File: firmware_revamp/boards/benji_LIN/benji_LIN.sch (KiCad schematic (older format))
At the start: 37 parts, among them J1 CONN_02X03, J2 Conn_01x11, J3 Conn_01x11, J4 CONN_01X03, J5 CONN_01x02, J6 CONN_01X03, SW1 SW_Push_SPST_NO, U1 MCP2561-E_SN, U2 ATMEGA16M1, U3 TLIN1021DRQ1, Y1 Crystal_SMD

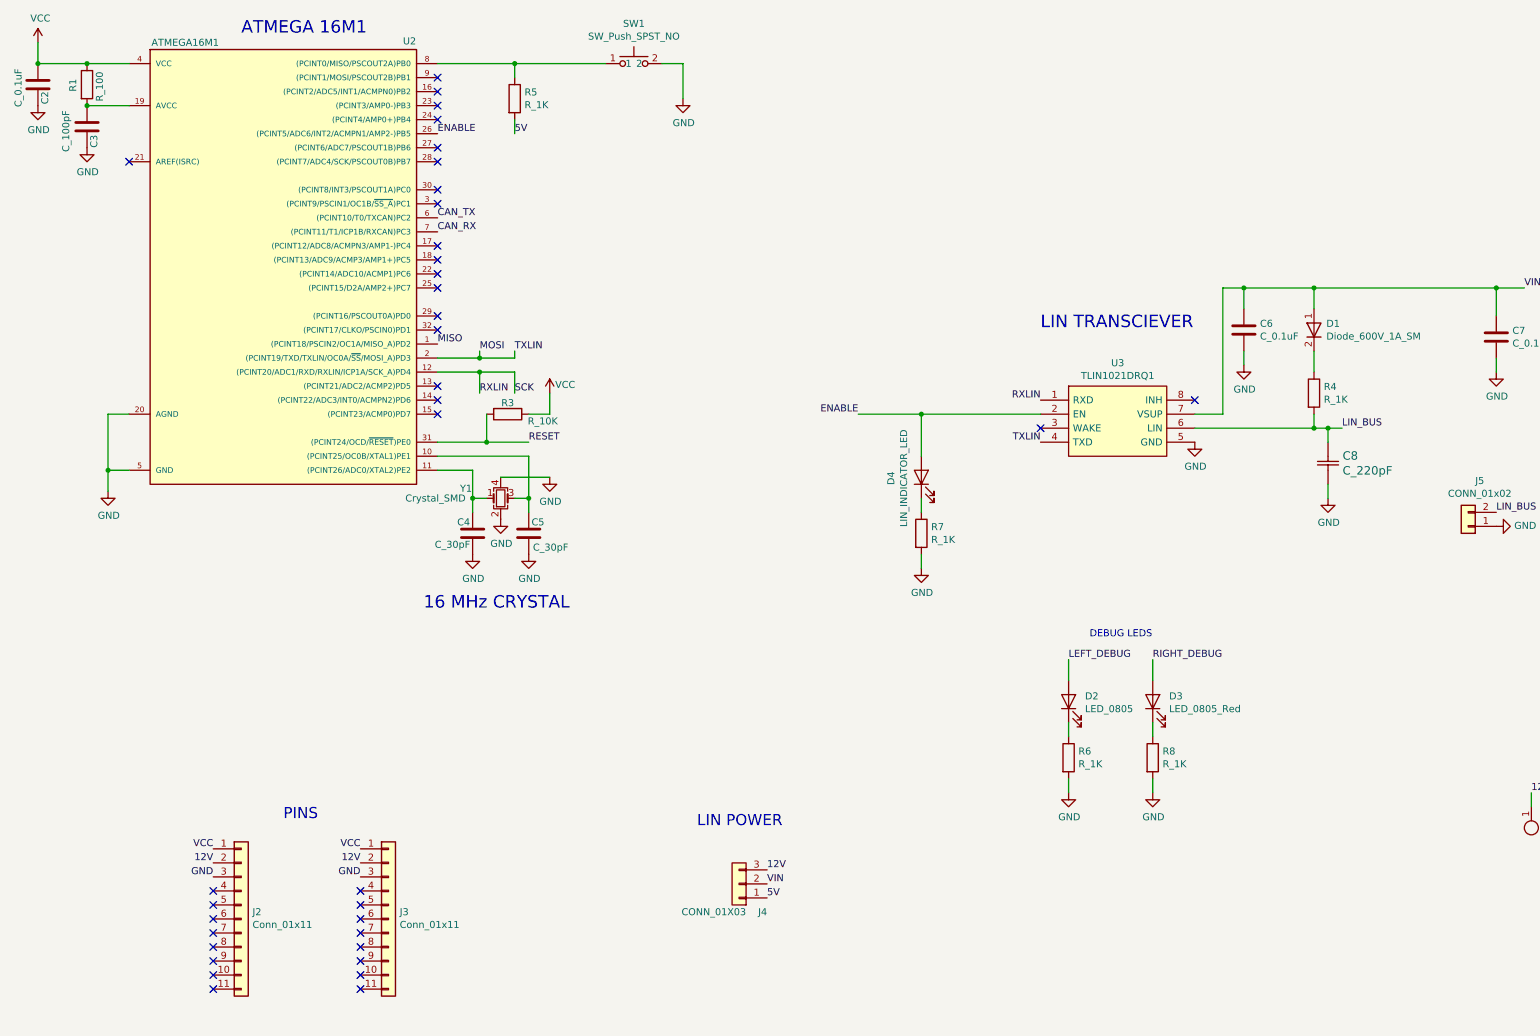
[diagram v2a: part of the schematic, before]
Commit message: Amended and finished up layout
assigned pins to headers, changed diode to led on LIN transciever
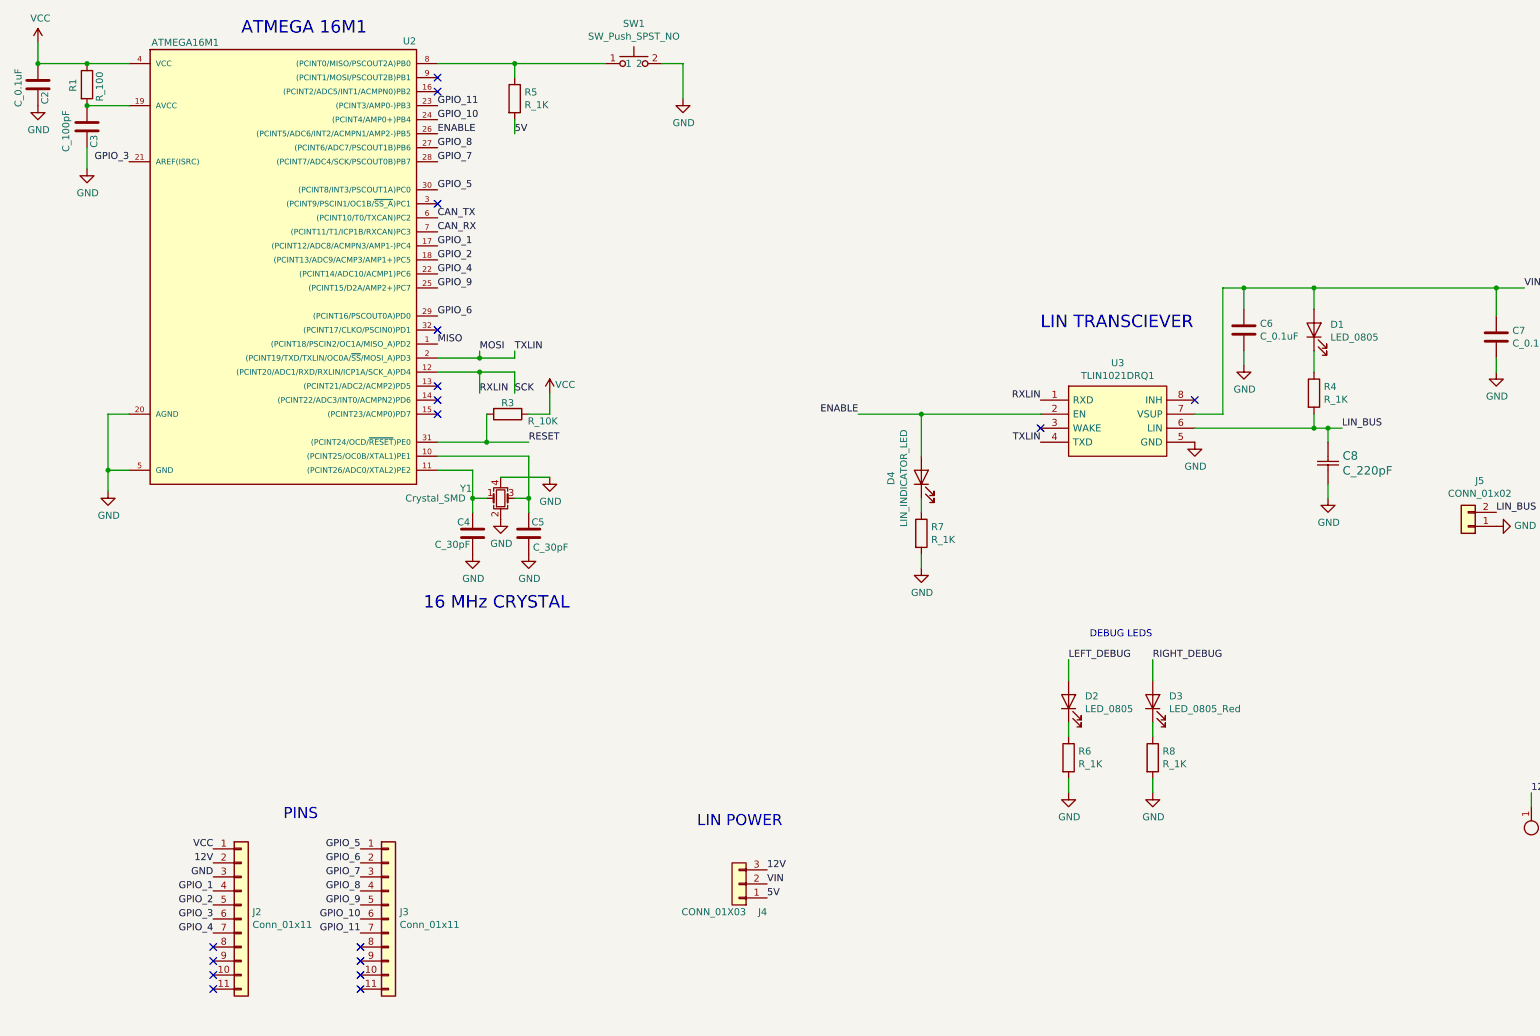
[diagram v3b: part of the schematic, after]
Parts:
- removed D1: Diode_600V_1A_SM, footprints:Diode_600V_1A_SM, symbol formula:Diode_600V_1A_SM
- added D1: LED_0805, footprints:LED_0805_OEM, symbol formula:LED_0805
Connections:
- net 12V: no longer J3.2
- net GND: no longer J3.3
- net VCC: no longer J3.1
- net VIN: now also D1.2 (A)
- net GPIO_1: now reaches U2.17 ((PCINT12/ADC8/ACMPN3/AMP1-)PC4)
- net GPIO_1: now also J2.4
- net GPIO_2: now reaches U2.18 ((PCINT13/ADC9/ACMP3/AMP1+)PC5)
- net GPIO_2: now also J2.5
- net GPIO_3: now reaches U2.21 (AREF(ISRC))
- net GPIO_3: now also J2.6
- net GPIO_4: now reaches U2.22 ((PCINT14/ADC10/ACMP1)PC6)
- net GPIO_4: now also J2.7
- net GPIO_11: now reaches U2.23 ((PCINT3/AMP0-)PB3)
- net GPIO_11: now also J3.7
- net GPIO_10: now reaches U2.24 ((PCINT4/AMP0+)PB4)
- net GPIO_10: now also J3.6
- net GPIO_9: now reaches U2.25 ((PCINT15/D2A/AMP2+)PC7)
- net GPIO_9: now also J3.5
- net GPIO_8: now reaches U2.27 ((PCINT6/ADC7/PSCOUT1B)PB6)
- net GPIO_8: now also J3.4
- net GPIO_7: now reaches U2.28 ((PCINT7/ADC4/SCK/PSCOUT0B)PB7)
- net GPIO_7: now also J3.3
- net GPIO_6: now reaches U2.29 ((PCINT16/PSCOUT0A)PD0)
- net GPIO_6: now also J3.2
- net GPIO_5: now reaches U2.30 ((PCINT8/INT3/PSCOUT1A)PC0)
- net GPIO_5: now also J3.1
- net at R4.1: now also D1.1 (K)
- no-connect marks 37 -> 18
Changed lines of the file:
@@
 L power:GND #PWR04
 U 1 1 5D591138
-P 1150 1600
-F 0 "#PWR04" H 1150 1350 50  0001 C CNN
-F 1 "GND" H 1155 1427 50  0000 C CNN
-F 2 "" H 1150 1600 50  0001 C CNN
-F 3 "" H 1150 1600 50  0001 C CNN
-	1    1150 1600
+P 1150 1750
+F 0 "#PWR04" H 1150 1500 50  0001 C CNN
+F 1 "GND" H 1155 1577 50  0000 C CNN
+F 2 "" H 1150 1750 50  0001 C CNN
+F 3 "" H 1150 1750 50  0001 C CNN
+	1    1150 1750
 	1    0    0    -1
 $EndComp
@@
 Wire Wire Line
 	1300 3900 1300 3500
-NoConn ~ 1450 1700
 Wire Wire Line
 	3900 4200 3900 4100
@@
 Wire Wire Line
 	9900 3050 9900 3200
-$Comp
-L formula:Diode_600V_1A_SM D1
-U 1 1 603D587E
-P 9900 2900
-F 0 "D1" V 9854 2988 50  0000 L CNN
-F 1 "Diode_600V_1A_SM" V 9945 2988 50  0000 L CNN
-F 2 "footprints:Diode_600V_1A_SM" H 9850 3050 50  0001 C CNN
-F 3 "https://www.st.com/content/ccc/resource/technical/document/datasheet/c7/d5/fe/c4/56/21/41/02/CD00005135.pdf/files/CD00005135.pdf/jcr:content/translations/en.CD00005135.pdf" H 9850 3050 50  0001 C CNN
-F 4 "https://www.digikey.com/product-detail/en/stmicroelectronics/STTH1R06A/497-3765-1-ND/691935" H 9900 3100 50  0001 C CNN "Purchasing Link"
-	1    9900 2900
-	0    1    1    0
-$EndComp
 Connection ~ 11200 2600
 Wire Wire Line
@@
 	8750 6200 8750 6100
 $Comp
-L formula:Conn_01x11 J2
-U 1 1 603F6805
-P 2250 7150
-F 0 "J2" H 2330 7250 50  0000 L CNN
-F 1 "Conn_01x11" H 2330 7159 50  0000 L CNN
-F 2 "footprints:PinHeader_1x11_P2.54mm_Vertical" H 2150 7850 50  0001 C CNN
-F 3 "" H 2250 7150 50  0001 C CNN
-	1    2250 7150
-	1    0    0    -1
-$EndComp
-$Comp
 L formula:Conn_01x11 J3
 U 1 1 6040C0B1
@@
 Text Label 6650 3500 2    50   ~ 0
 ENABLE
-NoConn ~ 3650 1700
 NoConn ~ 3650 1100
 NoConn ~ 3650 1200
-NoConn ~ 3650 1300
-NoConn ~ 3650 1400
-NoConn ~ 3650 1600
-NoConn ~ 3650 1900
 NoConn ~ 3650 2000
-NoConn ~ 3650 2300
-NoConn ~ 3650 2400
-NoConn ~ 3650 2500
-NoConn ~ 3650 2600
 NoConn ~ 3650 2900
-NoConn ~ 3650 2800
 Text Label 3650 3000 0    50   ~ 0
 MISO
@@
 Text Label 2050 6800 2    50   ~ 0
 GND
-Text Label 3100 6600 2    50   ~ 0
-VCC
-Text Label 3100 6800 2    50   ~ 0
-GND
-NoConn ~ 3100 6900
-NoConn ~ 3100 7000
-NoConn ~ 3100 7100
-NoConn ~ 3100 7200
 NoConn ~ 3100 7300
 NoConn ~ 3100 7400
@@
 NoConn ~ 2050 7400
 NoConn ~ 2050 7300
-NoConn ~ 2050 7200
-NoConn ~ 2050 7100
-NoConn ~ 2050 7000
-NoConn ~ 2050 6900
 Connection ~ 4200 1000
 Wire Wire Line
@@
 	0    -1   -1   0
 $EndComp
-Text Label 3100 6700 2    50   ~ 0
-12V
 Text Label 2050 6700 2    50   ~ 0
 12V
+$Comp
+L formula:LED_0805 D1
+U 1 1 605B388F
+P 9900 2900
+F 0 "D1" V 9939 2783 50  0000 R CNN
+F 1 "LED_0805" V 9848 2783 50  0000 R CNN
+F 2 "footprints:LED_0805_OEM" H 9800 2900 50  0001 C CNN
+F 3 "http://www.osram-os.com/Graphics/XPic9/00078860_0.pdf" H 9900 3000 50  0001 C CNN
+F 4 "DK" H 9900 2900 60  0001 C CNN "MFN"
+F 5 "475-1410-1-ND" H 9900 2900 60  0001 C CNN "MPN"
+F 6 "https://www.digikey.com/products/en?keywords=475-1410-1-ND" H 10300 3400 60  0001 C CNN "PurchasingLink"
+	1    9900 2900
+	0    -1   -1   0
+$EndComp
+Text Label 1450 1700 2    50   ~ 0
+GPIO_3
+Wire Wire Line
+	1150 1600 1150 1750
+Text Label 3650 2500 0    50   ~ 0
+GPIO_4
+Text Label 3650 1300 0    50   ~ 0
+GPIO_11
+Text Label 3650 1400 0    50   ~ 0
+GPIO_10
+Text Label 3650 2300 0    50   ~ 0
+GPIO_1
+Text Label 3650 2400 0    50   ~ 0
+GPIO_2
+Text Label 3650 1900 0    50   ~ 0
+GPIO_5
+Text Label 3650 2800 0    50   ~ 0
+GPIO_6
+Text Label 3650 1700 0    50   ~ 0
+GPIO_7
+Text Label 3650 1600 0    50   ~ 0
+GPIO_8
+Text Label 3650 2600 0    50   ~ 0
+GPIO_9
+$Comp
+L formula:Conn_01x11 J2
+U 1 1 603F6805
+P 2250 7150
+F 0 "J2" H 2330 7250 50  0000 L CNN
+F 1 "Conn_01x11" H 2330 7159 50  0000 L CNN
+F 2 "footprints:PinHeader_1x11_P2.54mm_Vertical" H 2150 7850 50  0001 C CNN
+F 3 "" H 2250 7150 50  0001 C CNN
+	1    2250 7150
+	1    0    0    -1
+$EndComp
+Text Label 2050 6900 2    50   ~ 0
+GPIO_1
+Text Label 2050 7000 2    50   ~ 0
+GPIO_2
+Text Label 2050 7100 2    50   ~ 0
+GPIO_3
+Text Label 2050 7200 2    50   ~ 0
+GPIO_4
+Text Label 3100 6600 2    50   ~ 0
+GPIO_5
+Text Label 3100 6700 2    50   ~ 0
+GPIO_6
+Text Label 3100 6800 2    50   ~ 0
+GPIO_7
+Text Label 3100 6900 2    50   ~ 0
+GPIO_8
+Text Label 3100 7000 2    50   ~ 0
+GPIO_9
+Text Label 3100 7100 2    50   ~ 0
+GPIO_10
+Text Label 3100 7200 2    50   ~ 0
+GPIO_11
 $EndSCHEMATC
